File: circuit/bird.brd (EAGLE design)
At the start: 30.5 x 34 mm, 10 parts, among them U1 ATTINY84-20SSU

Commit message: add LED
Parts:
- added LED1: red, led:LED5MM
- added R1: 500, rcl:R1206
- moved REED_SWITCH 3.81 mm to (5.08, 22.9)
- moved C1 3.81 mm to (17.8, 22.9)
- moved LID_SERVO 2.54 mm to (5.08, 14.0)
- moved POWER_IN 1.27 mm to (5.08, 5.08)
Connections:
- new net INDICATOR: LED1.K, U1.11
- new net N$1: LED1.A, R1.1
- net 5V: now also R1.2
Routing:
- net INDICATOR: track 0.00 -> 32.7 mm
- net 5V: track 61.1 -> 88.2 mm, vias 1 -> 0
- net N$1: track 0.00 -> 12.2 mm
- net MOSI/CHARACTER_SERVO: track 42.9 -> 54.3 mm
- net MISO/ROLL_SERVO: track 45.6 -> 35.2 mm, vias 0 -> 1
- net GND: track 92.8 -> 85.4 mm, vias 0 -> 1
- net SCK: track 21.4 -> 27.5 mm
- net MAGNETIC_SENSOR: track 20.8 -> 14.7 mm
- net START_BUTTON: track 19.3 -> 17.0 mm, vias 0 -> 1
- net LID_SERVO: track 7.70 -> 9.05 mm, vias 1 -> 0
- net RESET: track 17.8 -> 17.3 mm

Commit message: update circuit
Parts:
- removed REED_SWITCH: 22-27-2021-02, con-molex:6410-02
- added J1: 22-27-2031-03, con-molex:6410-03
- added R2, R3: 10k 1%, rcl:R0603
- moved SPEAKER 1.80 mm to (16.5, 3.81)
- moved POWER_IN 1.42 mm to (5.71, 3.81)
- moved LID_SERVO 1.27 mm to (5.08, 12.7)
- turned R1 to 0 degrees
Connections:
- removed net MISO/ROLL_SERVO: PROGRAMMING_HEADER.1, ROLLING_SERVO.1, U1.8
- removed net MOSI/CHARACTER_SERVO: CHARACTER_SERVO.1, PROGRAMMING_HEADER.4, U1.7
- new net CHARACTER_SERVO: CHARACTER_SERVO.1, U1.3
- new net MAGNETIC_REFERENCE: R2.2, R3.1, U1.10
- new net MISO: PROGRAMMING_HEADER.1, U1.8
- new net MOSI: PROGRAMMING_HEADER.4, U1.7
- new net ROLL_SERVO: ROLLING_SERVO.1, U1.2
- net 5V: now also J1.1, R2.1
- net GND: now also J1.2, R3.2; no longer REED_SWITCH.2
- net MAGNETIC_SENSOR: now also J1.3; no longer REED_SWITCH.1
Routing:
- net MOSI/CHARACTER_SERVO: track 54.3 -> 0.00 mm
- net MISO: track 0.00 -> 38.3 mm, vias 0 -> 1
- net MISO/ROLL_SERVO: track 35.2 -> 0.00 mm, vias 1 -> 0
- net MOSI: track 0.00 -> 30.5 mm, vias 0 -> 1
- net CHARACTER_SERVO: track 0.00 -> 29.6 mm, vias 0 -> 1
- net GND: track 85.4 -> 110.5 mm
- net ROLL_SERVO: track 0.00 -> 12.6 mm, vias 0 -> 1
- net MAGNETIC_REFERENCE: track 0.00 -> 12.6 mm, vias 0 -> 2
- net START_BUTTON: track 17.0 -> 29.5 mm
- net INDICATOR: track 32.7 -> 23.5 mm, vias 0 -> 1
- net MAGNETIC_SENSOR: track 14.7 -> 24.0 mm
- net 5V: track 88.2 -> 81.3 mm, vias 0 -> 1
- net LID_SERVO: track 9.05 -> 12.8 mm, vias 0 -> 1
- net TONE: track 10.6 -> 12.9 mm
- net SCK: track 27.5 -> 29.7 mm, vias 0 -> 2
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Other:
- board text added: "Magnetic Sensor"

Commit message: neaten board
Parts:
- moved POWER_IN 0.90 mm to (5.08, 4.45)
- moved C1 0.64 mm to (17.8, 23.5)
- moved R1 0.64 mm to (11.4, 23.5)
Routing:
- net 5V: track 81.3 -> 103.6 mm
- net CHARACTER_SERVO: track 29.6 -> 40.1 mm
- net MAGNETIC_SENSOR: track 24.0 -> 16.6 mm
- net GND: track 110.5 -> 104.6 mm, vias 1 -> 0
- net MOSI: track 30.5 -> 34.7 mm, vias 1 -> 0
- net N$1: track 10.2 -> 9.55 mm
- net SCK: track 29.7 -> 29.2 mm
- net RESET: track 17.2 -> 17.7 mm

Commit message: more board tweaks
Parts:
- moved R2 9.71 mm to (19.7, 15.9)
- moved R3 9.71 mm to (19.7, 12.1)
- moved U1 2.84 mm to (12.7, 14.0)
- moved LED1 1.91 mm to (6.99, 30.5)
- moved SPEAKER 1.42 mm to (17.8, 4.45)
- moved ROLLING_SERVO 1.27 mm to (25.4, 16.5)
- moved CHARACTER_SERVO 1.27 mm to (25.4, 26.7)
- moved POWER_IN 1.27 mm to (6.35, 4.45), turned to 0 degrees
- moved START_BUTTON 1.27 mm to (25.4, 6.35)
- moved J1 0.64 mm to (5.08, 22.2)
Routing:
- net RESET: track 17.7 -> 39.5 mm
- net MOSI: track 34.7 -> 53.8 mm
- net 5V: track 103.6 -> 87.1 mm
- net MISO: track 38.6 -> 29.0 mm, vias 1 -> 0
- net INDICATOR: track 23.6 -> 32.8 mm
- net START_BUTTON: track 29.6 -> 21.8 mm
- net SCK: track 29.2 -> 22.0 mm, vias 2 -> 0
- net LID_SERVO: track 13.3 -> 6.65 mm, vias 1 -> 0
- net ROLL_SERVO: track 12.6 -> 17.0 mm
- net CHARACTER_SERVO: track 40.1 -> 35.8 mm, vias 1 -> 0
- net MAGNETIC_REFERENCE: track 12.6 -> 10.3 mm
- net MAGNETIC_SENSOR: track 16.6 -> 17.5 mm, vias 1 -> 2
- net GND: track 104.6 -> 105.4 mm, vias 0 -> 1
- net N$1: track 9.55 -> 8.83 mm

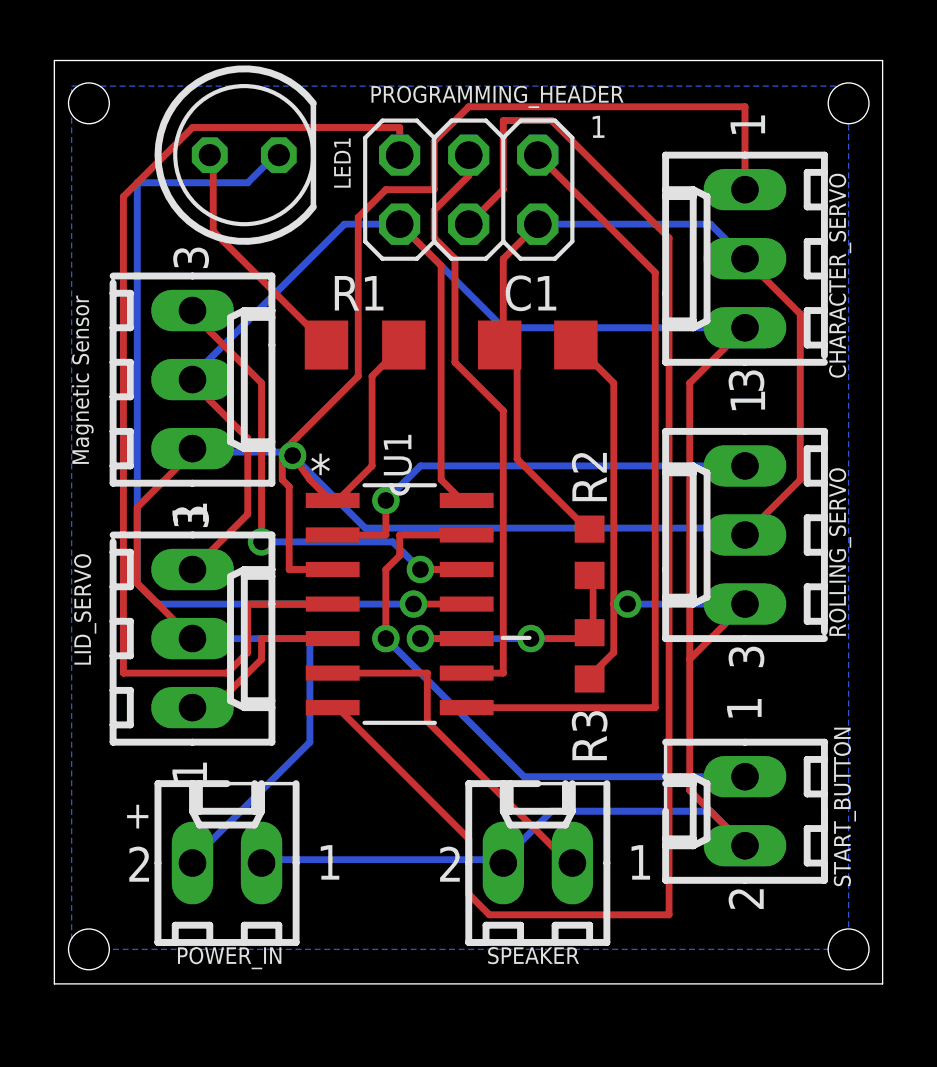
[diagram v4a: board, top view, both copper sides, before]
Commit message: fix trace
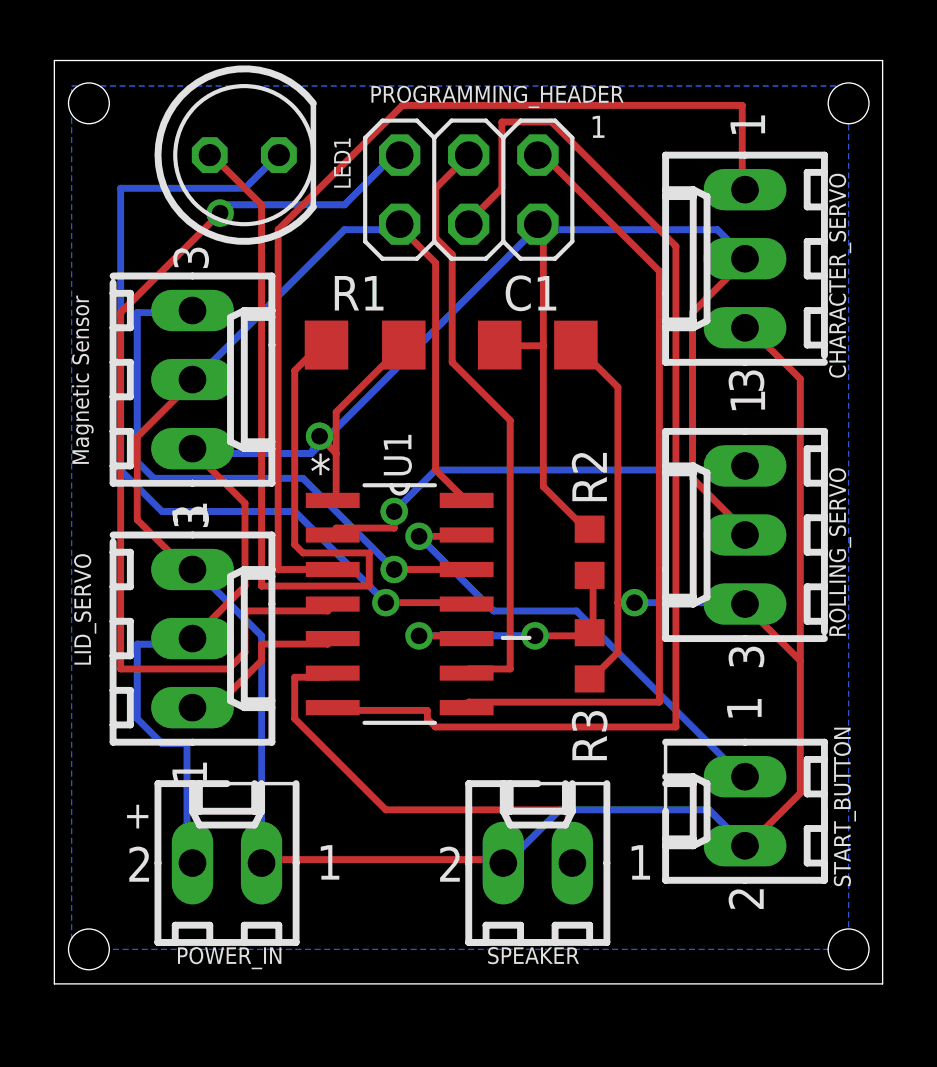
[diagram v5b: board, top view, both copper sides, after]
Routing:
- net N$1: track 8.83 -> 32.7 mm
- net MOSI: track 53.8 -> 43.3 mm
- net 5V: track 87.1 -> 79.1 mm
- net START_BUTTON: track 21.8 -> 17.4 mm
- net RESET: track 39.5 -> 35.5 mm, vias 0 -> 1
- net MAGNETIC_SENSOR: track 17.5 -> 21.3 mm, vias 2 -> 1
- net TONE: track 12.9 -> 16.5 mm
- net GND: track 105.4 -> 103.0 mm
- net INDICATOR: track 32.8 -> 31.4 mm
- net CHARACTER_SERVO: track 35.8 -> 36.6 mm

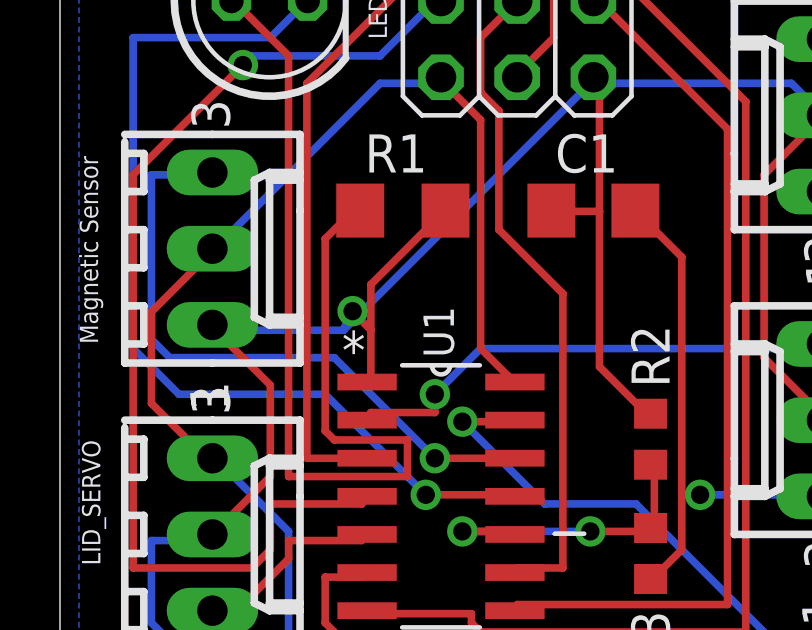
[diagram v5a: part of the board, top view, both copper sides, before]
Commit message: add servo
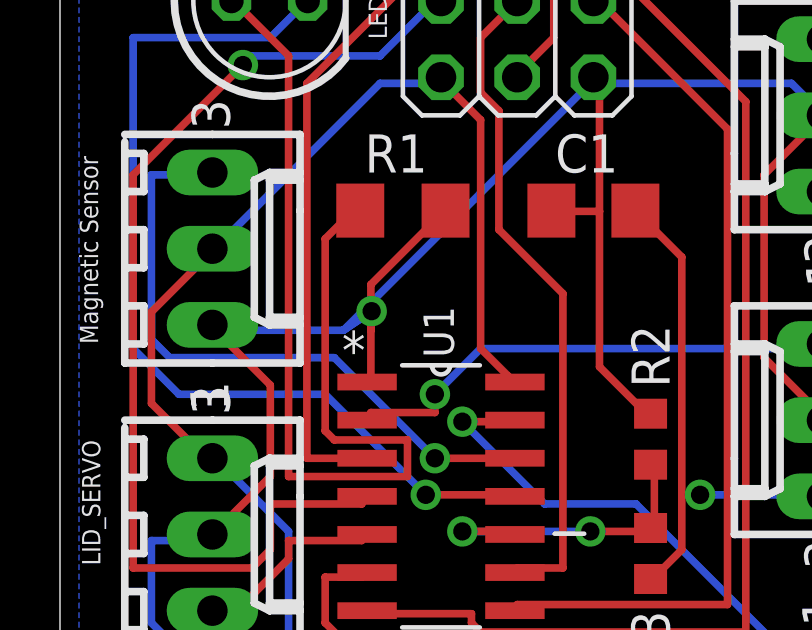
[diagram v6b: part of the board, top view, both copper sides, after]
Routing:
- net 5V: track 79.1 -> 79.7 mm
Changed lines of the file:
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@@
 <wire x1="5.1816" y1="19.5072" x2="5.08" y2="19.685" width="0.254" layer="1"/>
 <wire x1="5.1816" y1="12.8016" x2="5.08" y2="12.7" width="0.254" layer="1"/>
-<wire x1="9.7536" y1="20.1422" x2="10.3632" y2="19.5072" width="0.254" layer="1"/>
+<wire x1="10.3886" y1="20.1422" x2="10.3632" y2="19.5072" width="0.254" layer="1"/>
 <wire x1="5.1816" y1="19.5072" x2="9.4488" y2="19.5072" width="0.254" layer="16"/>
-<wire x1="9.4488" y1="19.5072" x2="9.7536" y2="20.1422" width="0.254" layer="16"/>
+<wire x1="9.4488" y1="19.5072" x2="10.3886" y2="20.1422" width="0.254" layer="16"/>
 <wire x1="5.1816" y1="19.5072" x2="5.08" y2="19.685" width="0.254" layer="16"/>
 <wire x1="9.4488" y1="19.5072" x2="17.6784" y2="27.7368" width="0.254" layer="16"/>
 <wire x1="17.6784" y1="27.7368" x2="17.78" y2="27.94" width="0.254" layer="16"/>
-<wire x1="9.4488" y1="19.5072" x2="9.7536" y2="20.1422" width="0.254" layer="16"/>
-<via x="9.7536" y="20.1422" extent="1-16" drill="0.6096"/>
+<wire x1="9.4488" y1="19.5072" x2="10.3886" y2="20.1422" width="0.254" layer="16"/>
+<via x="10.3886" y="20.1422" extent="1-16" drill="0.6096"/>
 </signal>
 <signal name="GND">

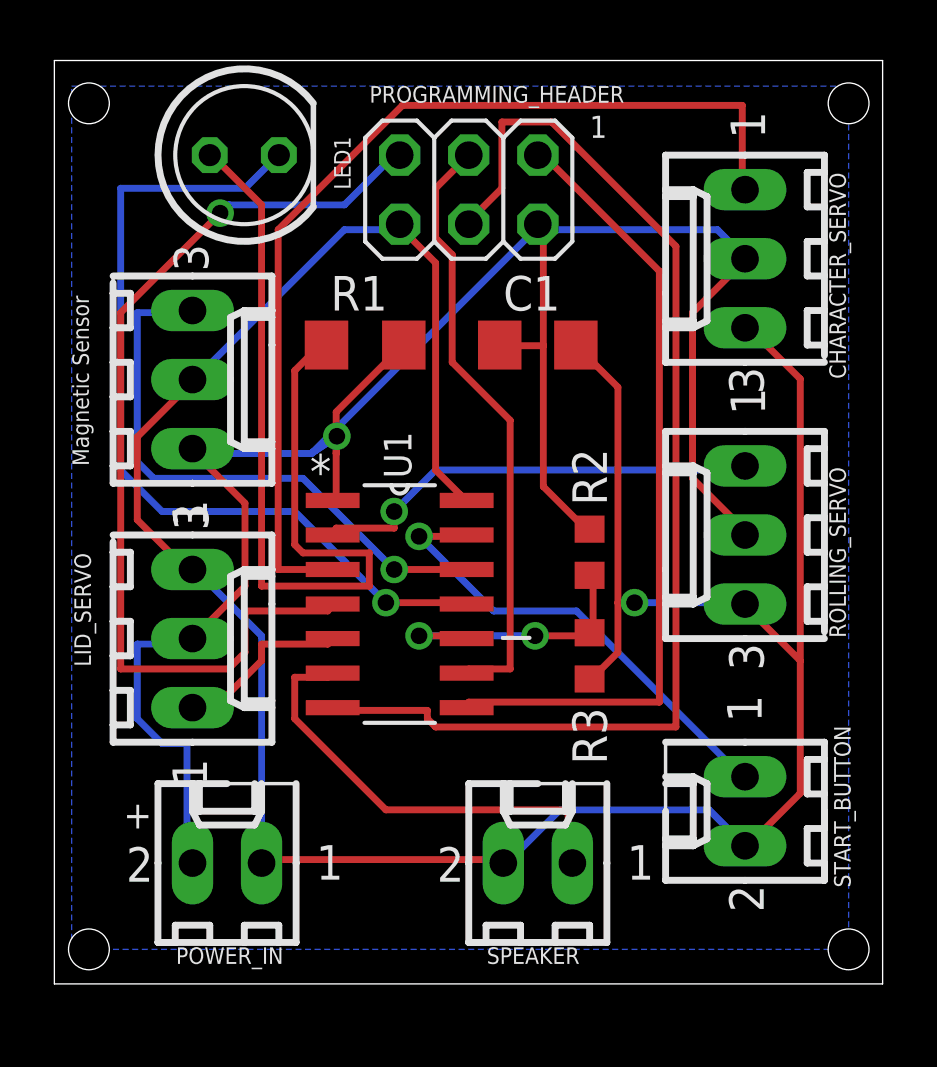
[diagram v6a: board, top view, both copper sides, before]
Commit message: add sensor
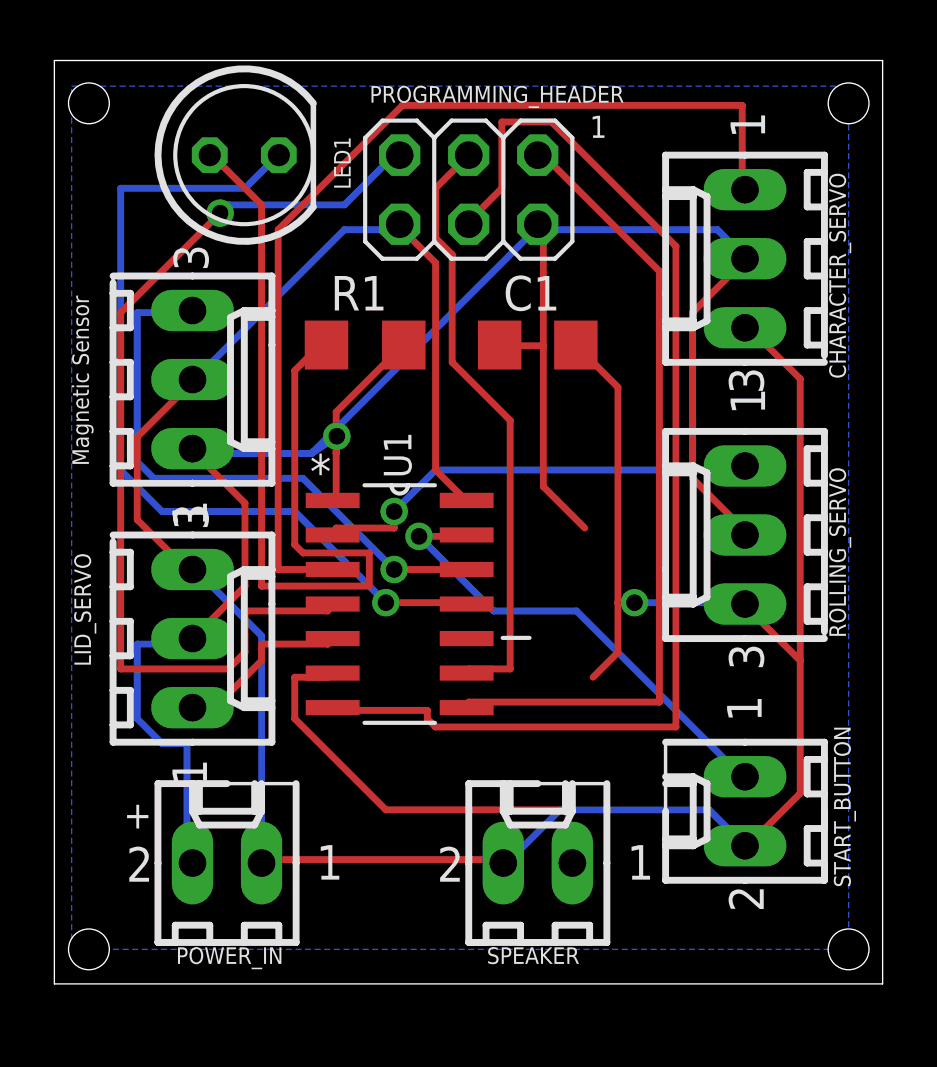
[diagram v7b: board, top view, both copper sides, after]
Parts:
- removed R2, R3: 10k 1%, rcl:R0603
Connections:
- removed net MAGNETIC_REFERENCE: R2.2, R3.1, U1.10
- net 5V: no longer R2.1
- net GND: no longer R3.2
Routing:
- net MAGNETIC_REFERENCE: track 10.3 -> 0.00 mm, vias 2 -> 0
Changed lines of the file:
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@@
 </element>
 <element name="R1" library="rcl" package="R1206" value="500" x="11.43" y="23.495"/>
-<element name="R2" library="rcl" package="R0603" value="10k 1%" x="19.685" y="15.875" smashed="yes" rot="R270">
-<attribute name="NAME" x="19.05" y="19.685" size="1.27" layer="25" rot="R270"/>
-<attribute name="VALUE" x="18.415" y="17.145" size="0.4064" layer="27" rot="R270"/>
-</element>
-<element name="R3" library="rcl" package="R0603" value="10k 1%" x="19.685" y="12.065" smashed="yes" rot="R270">
-<attribute name="NAME" x="19.05" y="10.16" size="1.27" layer="25" rot="R270"/>
-<attribute name="VALUE" x="18.415" y="12.7" size="0.4064" layer="27" rot="R270"/>
-</element>
 <element name="J1" library="con-molex" package="6410-03" value="22-27-2031-03" x="5.08" y="22.225" smashed="yes" rot="R270">
 <attribute name="OC_NEWARK" value="unknown" x="5.08" y="22.225" size="1.778" layer="27" rot="R270" display="off"/>
@@
 <contactref element="PROGRAMMING_HEADER" pad="2"/>
 <contactref element="R1" pad="2"/>
-<contactref element="R2" pad="1"/>
 <contactref element="J1" pad="1"/>
 <wire x1="23.4696" y1="18.5928" x2="25.2984" y2="16.764" width="0.254" layer="1"/>
@@
 <wire x1="17.9832" y1="27.7368" x2="17.9832" y2="23.4696" width="0.254" layer="1"/>
 <wire x1="17.9832" y1="23.4696" x2="17.9832" y2="18.288" width="0.254" layer="1"/>
-<wire x1="19.5072" y1="16.764" x2="19.685" y2="16.725" width="0.254" layer="1"/>
 <wire x1="17.9832" y1="27.7368" x2="17.78" y2="27.94" width="0.254" layer="1"/>
 <wire x1="17.9832" y1="23.4696" x2="16.4592" y2="23.4696" width="0.254" layer="1"/>
@@
 <vertex x="0.635" y="1.27"/>
 </polygon>
-<contactref element="R3" pad="2"/>
 <contactref element="J1" pad="2"/>
 <wire x1="3.048" y1="17.0688" x2="4.8768" y2="15.24" width="0.254" layer="1"/>
@@
 <wire x1="20.7264" y1="14.0208" x2="20.7264" y2="12.192" width="0.254" layer="1"/>
 <wire x1="19.2024" y1="23.4696" x2="20.7264" y2="21.9456" width="0.254" layer="1"/>
-<wire x1="19.812" y1="11.2776" x2="19.685" y2="11.215" width="0.254" layer="1"/>
 <wire x1="19.2024" y1="23.4696" x2="19.18" y2="23.495" width="0.254" layer="1"/>
 <wire x1="16.4592" y1="4.572" x2="7.62" y2="4.572" width="0.254" layer="1"/>
@@
 <via x="12.192" y="14.0208" extent="1-16" drill="0.6096"/>
 </signal>
-<signal name="MAGNETIC_REFERENCE">
-<contactref element="U1" pad="10"/>
-<contactref element="R2" pad="2"/>
-<contactref element="R3" pad="1"/>
-<wire x1="19.812" y1="14.9352" x2="19.812" y2="13.1064" width="0.254" layer="1"/>
-<wire x1="19.812" y1="13.1064" x2="19.685" y2="12.915" width="0.254" layer="1"/>
-<wire x1="19.812" y1="14.9352" x2="19.685" y2="15.025" width="0.254" layer="1"/>
-<wire x1="17.6784" y1="12.8016" x2="19.5072" y2="12.8016" width="0.254" layer="1"/>
-<wire x1="13.4112" y1="12.8016" x2="17.6784" y2="12.8016" width="0.254" layer="16"/>
-<wire x1="14.9352" y1="12.8016" x2="13.4112" y2="12.8016" width="0.254" layer="1"/>
-<wire x1="19.5072" y1="12.8016" x2="19.685" y2="12.915" width="0.254" layer="1"/>
-<wire x1="14.9352" y1="12.8016" x2="15.1638" y2="12.7" width="0.254" layer="1"/>
-<via x="17.6784" y="12.8016" extent="1-16" drill="0.6096"/>
-<via x="13.4112" y="12.8016" extent="1-16" drill="0.6096"/>
-</signal>
 <signal name="ROLL_SERVO">
